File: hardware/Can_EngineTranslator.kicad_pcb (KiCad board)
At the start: 2 copper layers, 55 parts, among them J2 Screw_Terminal_01x02, J3 Screw_Terminal_01x02, J4 Screw_Terminal_01x02, J5 Screw_Terminal_01x02, J6 Conn_01x06_Male, J7 Screw_Terminal_01x02, SW1 SW_Push, U1 STM32F105RBTx, U2 LM2596S-5, U3 LM1117-3.3, U4 MCP2562-H-SN, U5 MCP2562-H-SN, Y1 Crystal 8 MHz

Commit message: Sync with Podio
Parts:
- removed J4, J7: Screw_Terminal_01x02, TerminalBlock:TerminalBlock_bornier-2_P5.08mm
- removed J6: Conn_01x06_Male, Connector_PinHeader_2.54mm:PinHeader_1x06_P2.54mm_Vertical
- added C17: CP_Small, Capacitor_SMD:C_1206_3216Metric, F.Cu at (75.5, 46.4)
- added C18: CP_Small, Capacitor_SMD:C_1206_3216Metric, F.Cu at (75.5, 52.2)
- added C19: 100nF, Capacitor_SMD:C_0805_2012Metric, F.Cu at (85.2, 70.1)
- added C20: 100nF, Capacitor_SMD:C_0805_2012Metric, F.Cu at (86.9, 82.2)
- added FB1: Ferrite_Bead_Small, Resistor_SMD:R_1206_3216Metric, F.Cu at (75.4, 49.3)
- added J1: ProgramerConnector, Connector_PinHeader_2.54mm:PinHeader_1x06_P2.54mm_Vertical, F.Cu at (88.0, 93.0)
- added JP1: Jumper, Connector_PinHeader_2.54mm:PinHeader_1x02_P2.54mm_Vertical, F.Cu at (81.0, 87.0)
- added JP2: Jumper, Connector_PinHeader_2.54mm:PinHeader_1x02_P2.54mm_Vertical, F.Cu at (80.0, 75.3)
- added Q1: BSS138, Package_TO_SOT_SMD:SOT-23, F.Cu at (69.3, 65.8)
- added R12: 100, Resistor_SMD:R_1206_3216Metric, F.Cu at (74.3, 67.6)
- added R13: 10k, Resistor_SMD:R_1206_3216Metric, F.Cu at (74.1, 64.9)
- C1, C2: value 100nF -> 22pF; moved to F.Cu
- C10: value 100nF -> 680uF; footprint Capacitor_SMD:C_0805_2012Metric -> Capacitor_SMD:CP_Elec_6.3x7.7
- C11: value 220u -> 100nF; footprint Capacitor_SMD:CP_Elec_6.3x7.7 -> Capacitor_SMD:C_0805_2012Metric
- C14: value 122pF -> 220u; footprint Capacitor_SMD:C_0805_2012Metric -> Capacitor_SMD:CP_Elec_6.3x7.7; moved to F.Cu
- C15: value 22pF -> 100nF; moved to F.Cu
- C16, C3, C4, C5, C6, D10, L1, SW1, U1: moved to F.Cu
- C7: value 100u -> 100nF; footprint Capacitor_SMD:CP_Elec_6.3x7.7 -> Capacitor_SMD:C_0805_2012Metric
- D11, D12: value LED -> PESD2CAN.215; footprint LED_SMD:LED_0805_2012Metric -> Package_TO_SOT_SMD:SOT-23; moved to F.Cu
- D2: value D_Schottky -> LED; footprint Diode_SMD:D_SMB -> LED_SMD:LED_0805_2012Metric
- D4, D5: value PESD2CAN.215 -> LED; footprint Package_TO_SOT_SMD:SOT-23 -> LED_SMD:LED_0805_2012Metric
- D6: value D_Zener -> LED; footprint Diode_SMD:D_SMB -> LED_SMD:LED_0805_2012Metric
- D7: value LED -> 1SMA5937BT3G; footprint LED_SMD:LED_0805_2012Metric -> Diode_SMD:D_SMB; moved to F.Cu
- D8, D9: value LED -> SS24T3G; footprint LED_SMD:LED_0805_2012Metric -> Diode_SMD:D_SMB; moved to F.Cu
- F1: footprint Fuse:Fuse_1206_3216Metric -> Diode_SMD:D_SMB
- J2: value Screw_Terminal_01x02 -> CANcarConnector; footprint TerminalBlock:TerminalBlock_bornier-2_P5.08mm -> Connector_Molex:Molex_Micro-Fit_3.0_43650-0200_1x02_P3.00mm_Horizontal
- J3: value Screw_Terminal_01x02 -> CANinverterConnector; footprint TerminalBlock:TerminalBlock_bornier-2_P5.08mm -> Connector_Molex:Molex_Micro-Fit_3.0_43650-0200_1x02_P3.00mm_Horizontal
- J5: value Screw_Terminal_01x02 -> PowerOutputConnector; footprint TerminalBlock:TerminalBlock_bornier-2_P5.08mm -> Connector_Molex:Molex_Micro-Fit_3.0_43650-0300_1x03_P3.00mm_Horizontal
- R1: value R_Small -> 10k; moved to F.Cu
- R10, R11: value R -> 120R; footprint Resistor_SMD:R_0805_2012Metric -> Resistor_SMD:R_1206_3216Metric; moved to F.Cu
- R2: value R -> 100k; footprint Resistor_SMD:R_0805_2012Metric -> Resistor_SMD:R_1206_3216Metric
- R3: value R -> 180; footprint Resistor_SMD:R_0805_2012Metric -> Resistor_SMD:R_1206_3216Metric
- R4, R5: value 120R -> 180; footprint Resistor_SMD:R_0805_2012Metric -> Resistor_SMD:R_1206_3216Metric
- R6, R7, R8, R9: value R -> 180; footprint Resistor_SMD:R_0805_2012Metric -> Resistor_SMD:R_1206_3216Metric; moved to F.Cu
- Y1: footprint Crystal:Crystal_HC49-U_Vertical -> Crystal:Crystal_SMD_HC49-SD; moved to F.Cu
- moved J3 167.0 mm to (70.4, 75.7)
- moved J2 161.5 mm to (70.4, 87.3)
- moved F1 158.0 mm to (75.1, 38.8), turned to 90 degrees
- moved J5 157.7 mm to (70.1, 45.0), turned to 90 degrees
- moved U2 143.1 mm to (84.9, 43.4), turned to 90 degrees
- moved C11 143.0 mm to (81.7, 56.0), turned to 270 degrees
- moved D7 141.1 mm to (73.1, 57.8), turned to 270 degrees
- moved C10 136.0 mm to (86.8, 59.6)
- moved D8 135.8 mm to (77.9, 57.8), turned to 270 degrees
- moved D12 128.2 mm to (74.7, 74.1), turned to 0 degrees
- moved D6 126.0 mm to (98.0, 66.2), turned to 90 degrees
- moved D11 124.3 mm to (75.0, 85.9), turned to 0 degrees
- moved R11 123.4 mm to (81.0, 78.6), turned to 0 degrees
- moved D9 121.5 mm to (93.2, 57.4), turned to 270 degrees
- moved R8 120.4 mm to (98.0, 61.0), turned to 270 degrees
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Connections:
- C1 pad 1: NRST -> Net-(C1-Pad1)
- C10 pad 1: SW_VDDtarget -> Net-(C10-Pad1)
- C11 pad 1: +5V -> Net-(C10-Pad1)
- C13 pad 1: +5V -> SW_VDDtarget
- C14 pad 1: Net-(C14-Pad1) -> +5V
- C15 pad 1: Net-(C15-Pad1) -> +5V
- C16 pad 1: SW_VDDtarget -> +5V
- C2 pad 1: SW_VDDtarget -> Net-(C2-Pad1)
- C3 pad 1: SW_VDDtarget -> NRST
- C7 pad 1: +12V -> SW_VDDtarget
- C8 pad 1: +12V -> SW_VDDtarget
- C9 pad 1: +5V -> SW_VDDtarget
- D1 pad 1: SW_GND -> Net-(D1-Pad1)
- D10 pad 1: Net-(D10-Pad1) -> SW_GND
- D11 pad 1: Net-(D11-Pad1) -> CANcar_L
- D11 pad 2: Net-(D11-Pad2) -> CANcar_H
- D12 pad 1: Net-(D12-Pad1) -> CANinverter_L
- D12 pad 2: Net-(D12-Pad2) -> CANinverter_H
- D2 pad 2: SW_GND -> Net-(D2-Pad2)
- D3 pad 1: SW_GND -> Net-(D3-Pad1)
- D4 pad 1: CANcar_L -> Net-(D4-Pad1)
- D4 pad 2: CANcar_H -> Net-(D4-Pad2)
- D5 pad 1: CANinverter_L -> Net-(D5-Pad1)
- D5 pad 2: CANinverter_H -> Net-(D5-Pad2)
- D6 pad 2: SW_GND -> Net-(D6-Pad2)
- D7 pad 1: Net-(D7-Pad1) -> Net-(C10-Pad1)
- D7 pad 2: Net-(D7-Pad2) -> SW_GND
- D8 pad 1: Net-(D8-Pad1) -> Net-(C10-Pad1)
- D8 pad 2: Net-(D8-Pad2) -> SW_GND
- D9 pad 2: Net-(D9-Pad2) -> SW_GND
- F1 pad 1: +12V -> Net-(C17-Pad1)
- F1 pad 2: Net-(D6-Pad1) -> VCC
- J2 pad 1: +5V -> CANcar_H
- J2 pad 2: SW_GND -> CANcar_L
- J3 pad 1: SW_VDDtarget -> CANinverter_H
- J3 pad 2: SW_GND -> CANinverter_L
- J5 pad 1: CANinverter_L -> buzzer_gnd
- J5 pad 2: CANinverter_H -> SW_GND
- L2 pad 1: Net-(D2-Pad1) -> Net-(D9-Pad1)
- R10 pad 1: Net-(D11-Pad2) -> Net-(JP1-Pad1)
- R10 pad 2: SW_VDDtarget -> CANcar_H
- R11 pad 1: Net-(D12-Pad2) -> Net-(JP2-Pad1)
- R11 pad 2: SW_VDDtarget -> CANinverter_H
- R2 pad 1: +12V -> SW_VDDtarget
- R2 pad 2: Net-(D1-Pad2) -> NRST
- R3 pad 1: +5V -> SW_VDDtarget
- R3 pad 2: Net-(D3-Pad2) -> Net-(D1-Pad2)
- R4 pad 1: CANcar_H -> SW_VDDtarget
- R4 pad 2: CANcar_L -> Net-(D2-Pad2)
- R5 pad 1: CANinverter_H -> SW_VDDtarget
- R5 pad 2: CANinverter_L -> Net-(D3-Pad2)
- R6 pad 1: Net-(D9-Pad2) -> SW_VDDtarget
- R6 pad 2: SW_VDDtarget -> Net-(D4-Pad2)
- R7 pad 1: Net-(D8-Pad2) -> SW_VDDtarget
- R7 pad 2: SW_VDDtarget -> Net-(D5-Pad2)
- R8 pad 1: Net-(D7-Pad2) -> SW_VDDtarget
- R8 pad 2: SW_VDDtarget -> Net-(D6-Pad2)
- R9 pad 1: SW_VDDtarget -> +5V
- U1 pad 11: Net-(U1-Pad11) -> buzzer
- U1 pad 21: Net-(D10-Pad1) -> Net-(D1-Pad1)
- U1 pad 22: Net-(D11-Pad1) -> Net-(D3-Pad1)
- U1 pad 23: Net-(D12-Pad1) -> Net-(D5-Pad1)
- U1 pad 26: Net-(U1-Pad26) -> Net-(D2-Pad1)
- U1 pad 27: Net-(U1-Pad27) -> Net-(D4-Pad1)
- U1 pad 28: Net-(U1-Pad28) -> Net-(D6-Pad1)
- U1 pad 38: Net-(D7-Pad1) -> Net-(U1-Pad38)
- U1 pad 39: Net-(D8-Pad1) -> Net-(U1-Pad39)
- U1 pad 40: Net-(D9-Pad1) -> Net-(U1-Pad40)
- U1 pad 5: Net-(C14-Pad1) -> Net-(C1-Pad1)
- U1 pad 6: Net-(C15-Pad1) -> Net-(C2-Pad1)
- U2 pad 1: +12V -> Net-(C10-Pad1)
- U2 pad 2: Net-(D2-Pad1) -> Net-(D9-Pad1)
- Y1 pad 1: Net-(C15-Pad1) -> Net-(C2-Pad1)
- Y1 pad 2: Net-(C14-Pad1) -> Net-(C1-Pad1)
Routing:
- net SWDIO: track 69.3 -> 11.8 mm, vias 1 -> 0
- net buzzer: track 0.00 -> 55.3 mm, vias 0 -> 2
- net SWCLK: track 59.0 -> 15.0 mm
- net +12V: track 42.1 -> 0.00 mm
- net Net-(D9-Pad1): track 5.35 -> 40.0 mm
- net +5V: track 101.1 -> 133.7 mm, vias 0 -> 3
- net Net-(D2-Pad1): track 40.6 -> 9.11 mm
- net CANcar_L: track 46.7 -> 17.8 mm
- net SW_GND: track 24.0 -> 51.5 mm, vias 10 -> 26
- net Net-(C10-Pad1): track 0.00 -> 26.3 mm
- net CANcar_H: track 49.8 -> 24.3 mm
- net CANcar_RX: track 32.3 -> 9.50 mm, vias 1 -> 0
- net CANinverter_RX: track 34.0 -> 11.2 mm, vias 1 -> 0
- net buzzer_gnd: track 0.00 -> 21.5 mm
- net Net-(D1-Pad1): track 0.00 -> 20.9 mm
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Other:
- board outline added: 72 x 63 mm
- board text added: "PUT Motorsport CAN translator M. Przydatek S. Sambor"

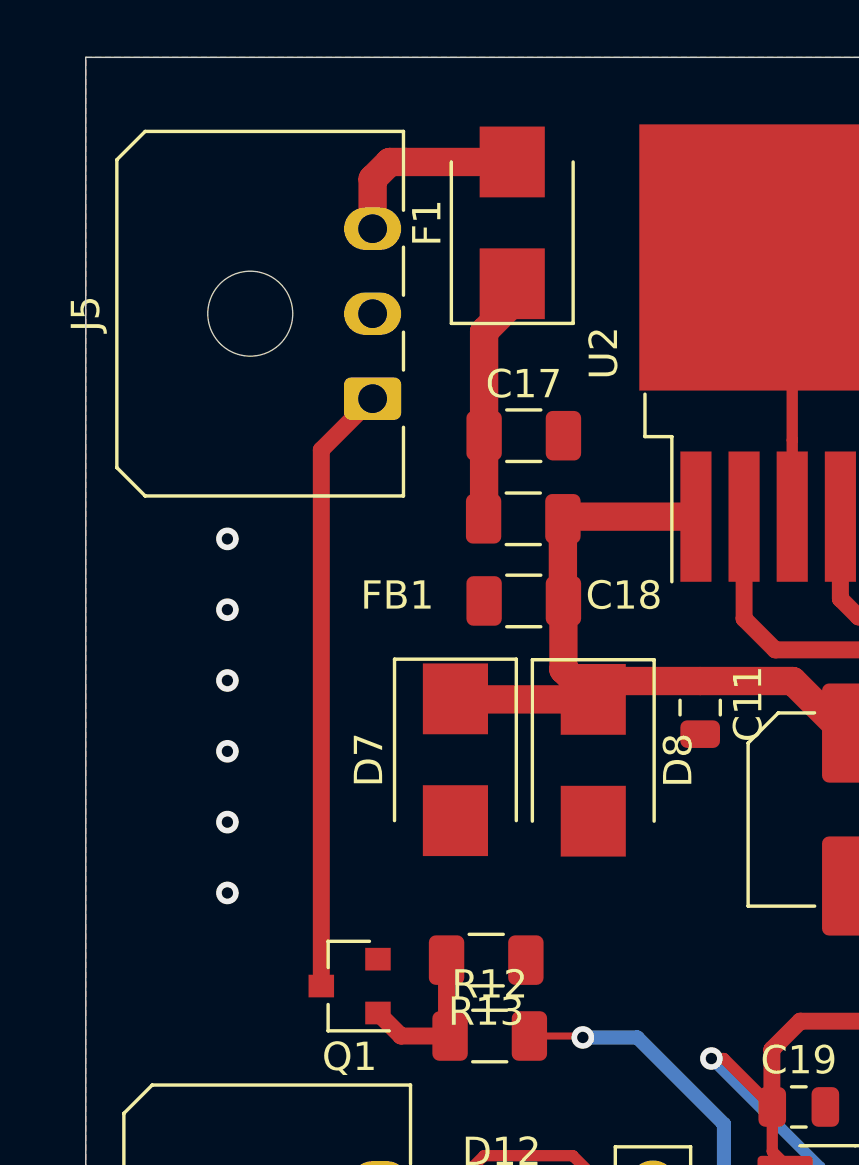
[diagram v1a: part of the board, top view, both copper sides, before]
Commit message: Connector change
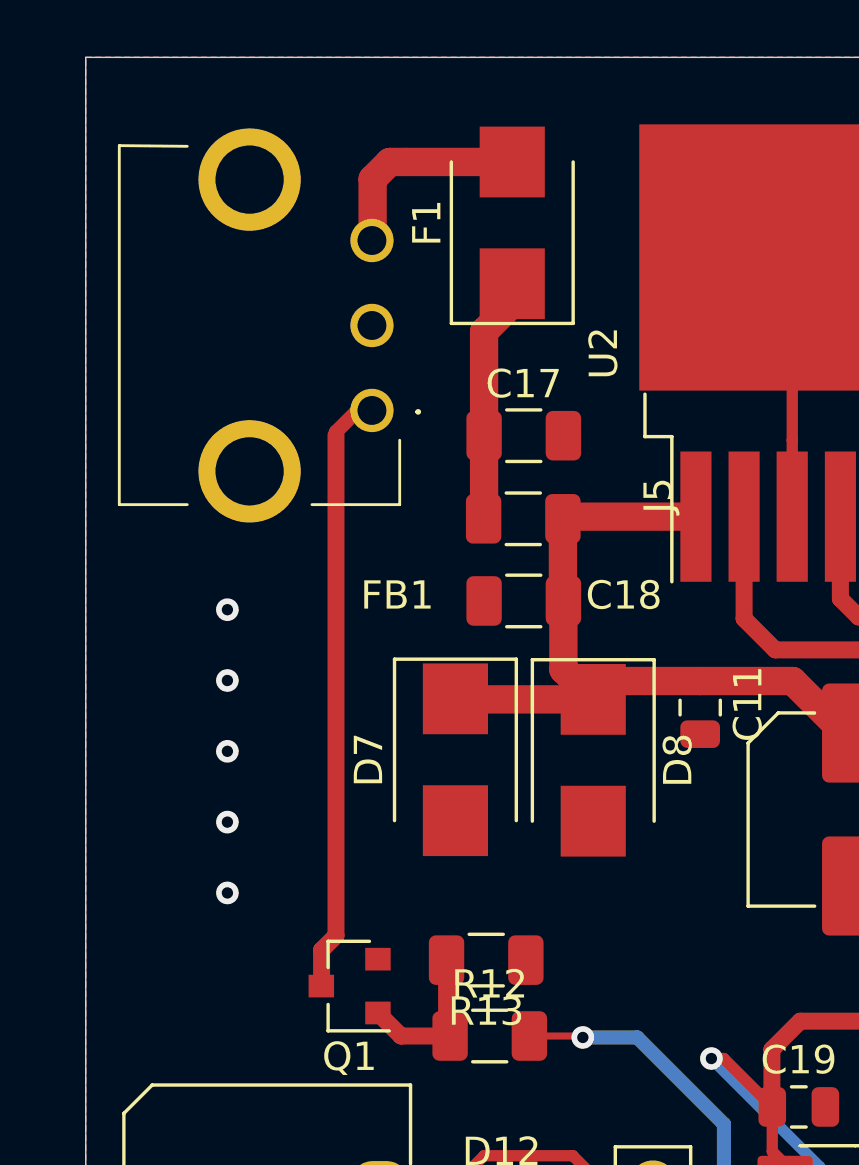
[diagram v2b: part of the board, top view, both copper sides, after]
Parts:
- J5: footprint Connector_Molex:Molex_Micro-Fit_3.0_43650-0300_1x03_P3.00mm_Horizontal -> lib:436500304
- moved J5 0.42 mm to (70.1, 45.5), turned to 270 degrees
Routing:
- net SW_GND: vias 26 -> 25

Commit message: Cosmetic changes to pcb
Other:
- board text added: "CLK"
- board text added: "DIO"
- board text added: "GND"
- board text added: "NRST"
- board text added: "Vdd"
